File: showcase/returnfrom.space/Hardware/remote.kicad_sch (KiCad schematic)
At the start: 113 parts, among them J23 USB_C_Receptacle_USB2.0_16P, J24 Conn_02x04_Odd_Even, J25 Conn_01x02, J27 Conn_01x02, J6 OLED, Q4 NPN, SW28 SW_SPST, SW29 SW_SPST, SW30 SW_SPST, SW31 SW_SPST, SW32 SW_SPST, SW33 SW_SPST, SW34 SW_SPST, SW35 SW_SPDT_321, SW36 BOOTSEL, SW37 RESET, U12 TP4056, U13 TLV62565DBVx, U14 FM8002, U15 LIS2DH, U17 LMA3722T421-OA5, U18 TLV2372, U2 ESP32-S2-MINI-1

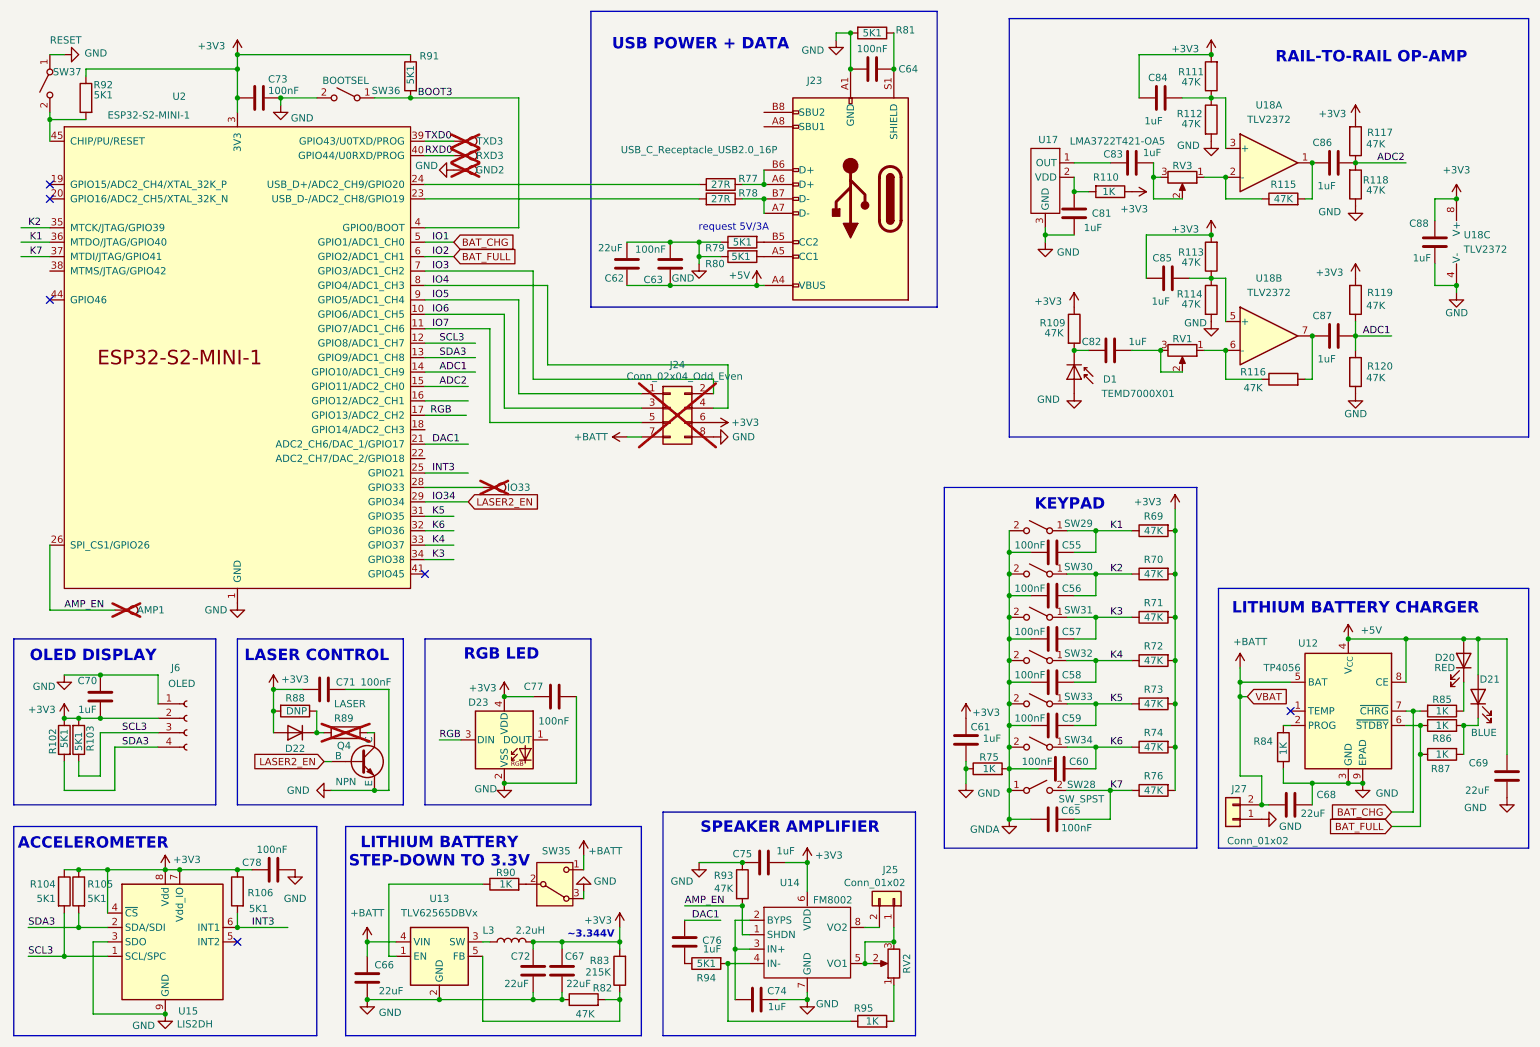
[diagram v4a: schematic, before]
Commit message: Done. Ordered 50pcs. TO DO: clean-up, add BOM & POS
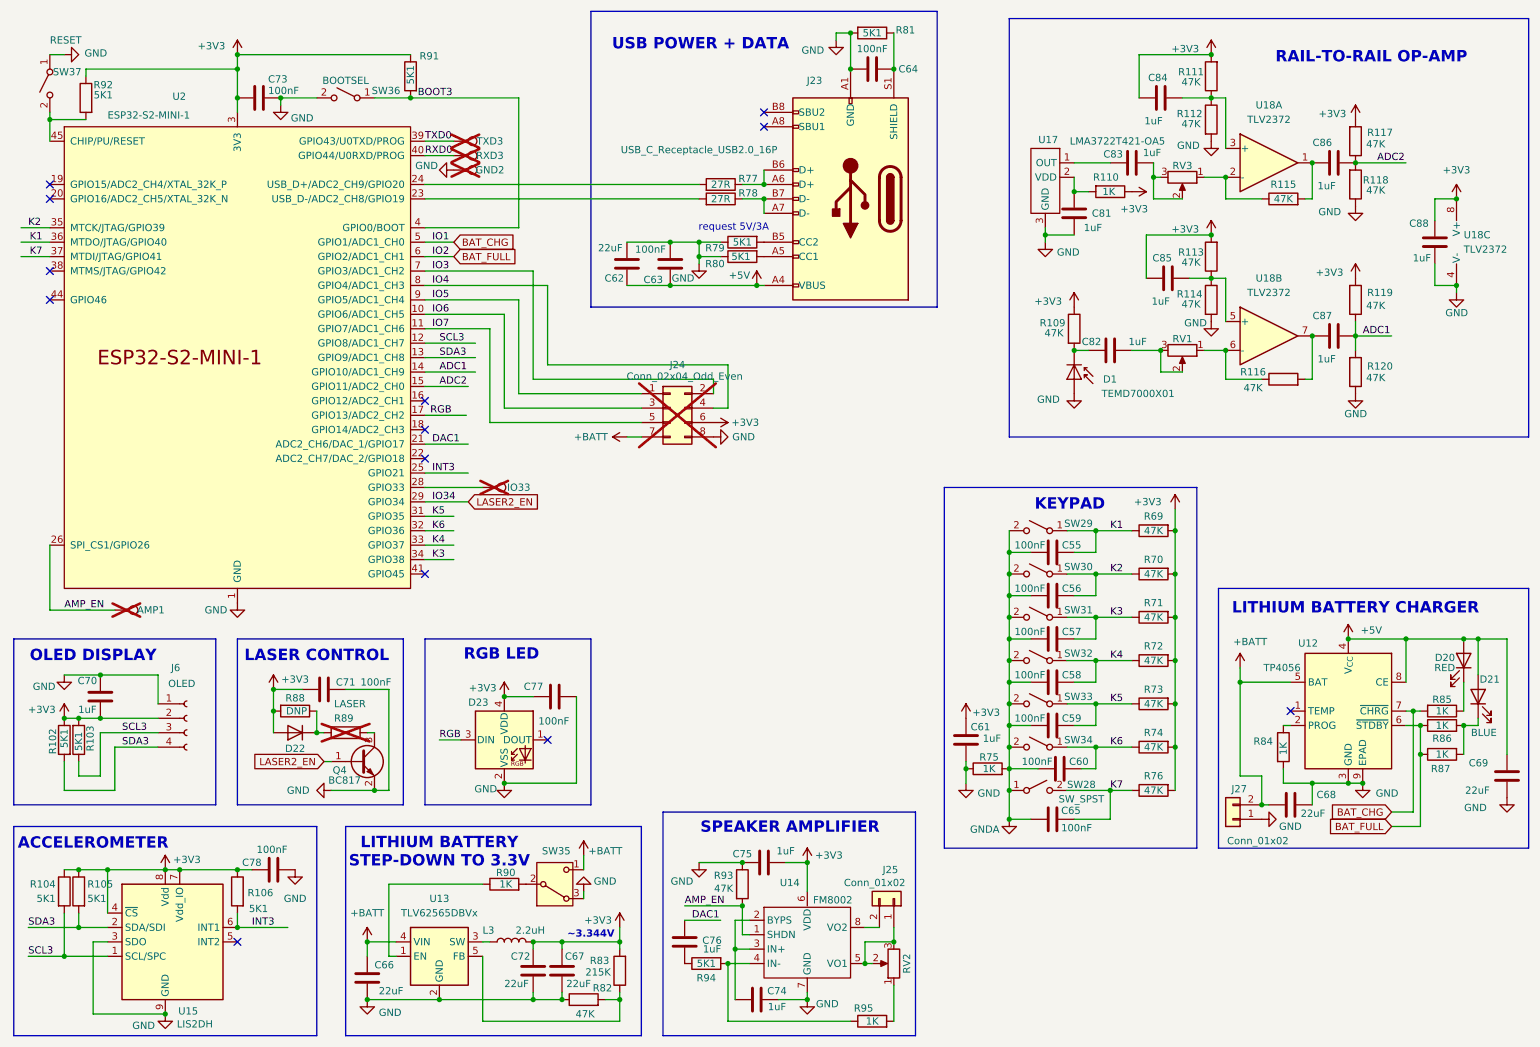
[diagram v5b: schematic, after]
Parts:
- removed Q4: NPN, Package_TO_SOT_SMD:SOT-23, symbol Simulation_SPICE:NPN
- added Q4: BC817, Package_TO_SOT_SMD:SOT-23, symbol Transistor_BJT:BC817
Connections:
- net GND: now also Q4.2 (E)
- net LASER2_EN: now also Q4.1 (B)
- net at R89.1: now also Q4.3 (C)
- no-connect marks 6 -> 13
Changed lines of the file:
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@@
 	)
 	(junction
-		(at 231.14 135.89)
+		(at 205.74 114.3)
 		(diameter 0)
 		(color 0 0 0 0)
 	)
 	(junction
-		(at 205.74 114.3)
+		(at 190.5 129.54)
 		(diameter 0)
 		(color 0 0 0 0)
 	)
 	(junction
-		(at 190.5 129.54)
+		(at 201.93 74.93)
 		(diameter 0)
 		(color 0 0 0 0)
 	)
 	(junction
-		(at 201.93 74.93)
+		(at 78.74 152.4)
 		(diameter 0)
 		(color 0 0 0 0)
@@
 	)
 	(junction
-		(at 78.74 152.4)
-		(diameter 0)
-		(color 0 0 0 0)
-	)
-	(junction
 		(at 190.5 152.4)
 		(diameter 0)
@@
 	)
 	(no_connect
+		(at 87.63 88.9)
+	)
+	(no_connect
 		(at 21.59 45.72)
 	)
 	(no_connect
+		(at 147.32 35.56)
+	)
+	(no_connect
 		(at 21.59 48.26)
 	)
@@
 	)
 	(no_connect
+		(at 21.59 60.96)
+	)
+	(no_connect
+		(at 109.22 143.51)
+	)
+	(no_connect
 		(at 21.59 66.04)
 	)
 	(no_connect
+		(at 147.32 33.02)
+	)
+	(no_connect
+		(at 87.63 83.82)
+	)
+	(no_connect
+		(at 87.63 93.98)
+	)
+	(no_connect
 		(at 240.03 138.43)
 	)
@@
 	(wire
 		(pts
-			(xy 231.14 133.35) (xy 231.14 135.89)
+			(xy 231.14 133.35) (xy 231.14 149.86)
 		)
 		(stroke
@@
 	(wire
 		(pts
-			(xy 231.14 135.89) (xy 232.41 135.89)
-		)
-		(stroke
-			(width 0)
-			(type default)
-		)
-	)
-	(wire
-		(pts
 			(xy 109.22 77.47) (xy 109.22 63.5)
 		)
@@
 	(wire
 		(pts
-			(xy 81.28 152.4) (xy 78.74 152.4)
-		)
-		(stroke
-			(width 0)
-			(type default)
-		)
-	)
-	(wire
-		(pts
 			(xy 144.78 180.34) (xy 142.24 180.34)
 		)
@@
 	(wire
 		(pts
-			(xy 87.63 83.82) (xy 95.25 83.82)
-		)
-		(stroke
-			(width 0)
-			(type default)
-		)
-	)
-	(wire
-		(pts
 			(xy 99.06 71.12) (xy 87.63 71.12)
 		)
@@
 	(wire
 		(pts
-			(xy 231.14 135.89) (xy 231.14 149.86)
-		)
-		(stroke
-			(width 0)
-			(type default)
-		)
-	)
-	(wire
-		(pts
 			(xy 162.56 25.4) (xy 162.56 19.05)
 		)
@@
 	(wire
 		(pts
+			(xy 78.74 152.4) (xy 81.28 152.4)
+		)
+		(stroke
+			(width 0)
+			(type default)
+		)
+	)
+	(wire
+		(pts
 			(xy 21.59 33.02) (xy 21.59 34.29)
 		)
@@
 		)
 	)
-	(global_label "VBAT"
-		(shape input)
-		(at 232.41 135.89 0)
-		(fields_autoplaced yes)
-		(effects
-			(font
-				(size 1.27 1.27)
-			)
-			(justify left)
-		)
-		(property "Intersheetrefs" "${INTERSHEET_REFS}"
-			(at 239.81 135.89 0)
-			(effects
-				(font
-					(size 1.27 1.27)
-				)
-				(justify left)
-				(hide yes)
-			)
-		)
-	)
 	(global_label "BAT_CHG"
 		(shape input)
@@
 	)
 	(symbol
+		(lib_id "Transistor_BJT:BC817")
+		(at 76.2 147.32 0)
+		(unit 1)
+		(exclude_from_sim no)
+		(in_bom yes)
+		(on_board yes)
+		(dnp no)
+		(property "Reference" "Q4"
+			(at 71.374 148.844 0)
+			(effects
+				(font
+					(size 1.27 1.27)
+				)
+				(justify left)
+			)
+		)
+		(property "Value" "BC817"
+			(at 70.612 150.622 0)
+			(effects
+				(font
+					(size 1.27 1.27)
+				)
+				(justify left)
+			)
+		)
+		(property "Footprint" "Package_TO_SOT_SMD:SOT-23"
+			(at 81.28 149.225 0)
+			(effects
+				(font
+					(size 1.27 1.27)
+					(italic yes)
+				)
+				(justify left)
+				(hide yes)
+			)
+		)
+		(property "Datasheet" "https://www.onsemi.com/pub/Collateral/BC818-D.pdf"
+			(at 76.2 147.32 0)
+			(effects
+				(font
+					(size 1.27 1.27)
+				)
+				(justify left)
+				(hide yes)
+			)
+		)
+		(property "Description" "0.8A Ic, 45V Vce, NPN Transistor, SOT-23"
+			(at 76.2 147.32 0)
+			(effects
+				(font
+					(size 1.27 1.27)
+				)
+				(hide yes)
+			)
+		)
+		(pin "3"
+		)
+		(pin "2"
+		)
+		(pin "1"
+		)
+		(instances
+			(project "spacescape"
+				(path "/418a52ba-b136-48f0-a485-149e9dc1363e/bd4ffa4f-b637-4be7-8de2-092b7a28716e"
+					(reference "Q4")
+					(unit 1)
+				)
+			)
+		)
+	)
+	(symbol
 		(lib_id "power:+5V")
 		(at 251.46 62.23 0)
@@
 					(unit 1)
 				)
-			)
-		)
-	)
-	(symbol
-		(lib_id "Simulation_SPICE:NPN")
-		(at 76.2 147.32 0)
-		(unit 1)
-		(exclude_from_sim no)
-		(in_bom yes)
-		(on_board yes)
-		(dnp no)
-		(property "Reference" "Q4"
-			(at 72.136 144.526 0)
-			(effects
-				(font
-					(size 1.27 1.27)
-				)
-				(justify left)
-			)
-		)
-		(property "Value" "NPN"
-			(at 71.882 150.876 0)
-			(effects
-				(font
-					(size 1.27 1.27)
-				)
-				(justify left)
-			)
-		)
-		(property "Footprint" "Package_TO_SOT_SMD:SOT-23"
-			(at 139.7 147.32 0)
-			(effects
-				(font
-					(size 1.27 1.27)
-				)
-				(hide yes)
-			)
-		)
-		(property "Datasheet" "https://ngspice.sourceforge.io/docs/ngspice-html-manual/manual.xhtml#cha_BJTs"
-			(at 139.7 147.32 0)
-			(effects
-				(font
-					(size 1.27 1.27)
-				)
-				(hide yes)
-			)
-		)
-		(property "Description" "Bipolar transistor symbol for simulation only, substrate tied to the emitter"
-			(at 76.2 147.32 0)
-			(effects
-				(font
-					(size 1.27 1.27)
-				)
-				(hide yes)
-			)
-		)
-		(property "Sim.Device" "NPN"
-			(at 76.2 147.32 0)
-			(effects
-				(font
-					(size 1.27 1.27)
-				)
-				(hide yes)
-			)
-		)
-		(property "Sim.Type" "GUMMELPOON"
-			(at 76.2 147.32 0)
-			(effects
-				(font
-					(size 1.27 1.27)
-				)
-				(hide yes)
-			)
-		)
-		(property "Sim.Pins" "1=C 2=B 3=E"
-			(at 76.2 147.32 0)
-			(effects
-				(font
-					(size 1.27 1.27)
-				)
-				(hide yes)
-			)
-		)
-		(pin "2"
-		)
-		(pin "1"
-		)
-		(pin "3"
-		)
-		(instances
-			(project "spacescape"
-				(path "/418a52ba-b136-48f0-a485-149e9dc1363e/bd4ffa4f-b637-4be7-8de2-092b7a28716e"
-					(reference "Q4")
-					(unit 1)
-				)
